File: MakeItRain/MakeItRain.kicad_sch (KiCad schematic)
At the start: 26 parts, among them IC1 OPA2340PA, IC2 LM2597MX-5.0_NOPB, J1 Conn_02x16_Odd_Even, J2 Conn_02x19_Odd_Even, J3 Conn_01x19, P1 Screw_Terminal_01x02, Q1 IRF9Z34NPBF, U1 178.6165.0001

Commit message: wip for hardware
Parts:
- removed C1, C2: 0.1uF, Capacitor_THT:C_Disc_D4.7mm_W2.5mm_P5.00mm, symbol Device:C
- removed C3: 68uF, Capacitor_THT:CP_Radial_D8.0mm_P3.50mm, symbol Device:CP1
- removed C4: 120uF, Capacitor_THT:CP_Radial_D8.0mm_P3.50mm, symbol Device:CP1
- removed D1: 1N5817, Diode_THT:D_DO-41_SOD81_P10.16mm_Horizontal, symbol Diode:1N5817
- removed IC1: OPA2340PA, SamacSys_Parts:DIP794W53P254L959H508Q8N, symbol SamacSys_Parts:OPA2340PA
- removed IC2: LM2597MX-5.0_NOPB, SamacSys_Parts:SOIC127P600X175-8N, symbol SamacSys_Parts:LM2597MX-5.0_NOPB
- removed IC?: LTV-846S, SOP254P1016X460-16N, symbol Samac_Sys:LTV-846S
- removed IC?: SN7404DR, SOIC127P600X175-14N, symbol Samac_Sys:SN7404DR
- removed L1: 150uH, Inductor_THT:L_Axial_L6.6mm_D2.7mm_P10.16mm_Horizontal_Vishay_IM-2, symbol Device:L
- removed P1: Screw_Terminal_01x02, TerminalBlock_Phoenix:TerminalBlock_Phoenix_MKDS-1,5-2-5.08_1x02_P5.08mm_Horizontal, symbol Connector:Screw_Terminal_01x02
- removed Q1: IRF9Z34NPBF, SamacSys_Parts:TO254P469X1042X1967-3P, symbol SamacSys_Parts:IRF9Z34NPBF
- removed R1, R6: 10k, Resistor_THT:R_Axial_DIN0207_L6.3mm_D2.5mm_P5.08mm_Vertical, symbol Device:R
- removed R5: 47k, Resistor_THT:R_Axial_DIN0207_L6.3mm_D2.5mm_P5.08mm_Vertical, symbol Device:R
- removed U1: 178.6165.0001, SamacSys_Parts:17861650001, symbol SamacSys_Parts:178.6165.0001
- added C9: 0.1uF, Capacitor_THT:C_Rect_L9.0mm_W3.6mm_P7.50mm_MKT, symbol Device:C
- added IC1: DS3231SN#, SamacSys_Parts:SOIC127P1032X265-16N, symbol SamacSys_Parts:DS3231SN#
- added U2: S8411-45R, SamacSys_Parts:S8411-45R_1, symbol SamacSys_Parts:S8411-45R
- R3: value 120k -> 10k; footprint Resistor_THT:R_Axial_DIN0207_L6.3mm_D2.5mm_P5.08mm_Vertical -> Resistor_THT:R_Axial_DIN0207_L6.3mm_D2.5mm_P2.54mm_Vertical
- R4: value 15k -> 10k; footprint Resistor_THT:R_Axial_DIN0207_L6.3mm_D2.5mm_P5.08mm_Vertical -> Resistor_THT:R_Axial_DIN0207_L6.3mm_D2.5mm_P2.54mm_Vertical
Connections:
- net +3V3: now also R3.1, R4.1, C9.1, IC1.2 (VCC)
- net +VDC: no longer R3.1
- net D4: no longer J3.13 (Pin_13)
- net GND: now also C9.2, IC1.10 (N.C._6), IC1.11 (N.C._7), IC1.12 (N.C._8), IC1.13 (GND), IC1.5 (N.C._1), IC1.6 (N.C._2), IC1.7 (N.C._3), IC1.8 (N.C._4), IC1.9 (N.C._5), U2.2 (-); no longer R4.2
- net SCL: now reaches R3.2
- net SCL: now also IC1.16 (SCL); no longer R4.1
- new net RTCBattLevel: IC1.14 (VBAT), U2.1 (+)
- new net SDA: IC1.15 (SDA), R4.2
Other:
- added sheet InputIsolation (InputIsolation.kicad_sch)
- added sheet Power (Power.kicad_sch)
- added sheet Voltage Sensors (VoltageSensors.kicad_sch)
- moved on the sheet: J1, J2, J3, R2, Z1, Z2, Z3, Z4

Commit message: wip
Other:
- sheet InputIsolation ports: added 1in, 1out, 2in, 2out, 3in, 3out, 4in, 4out; removed none
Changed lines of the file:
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@@
       (effects (font (size 1.27 1.27)) (justify left top))
+    )
+    (pin "2out" input (at 146.05 59.69 0)
+      (effects (font (size 1.27 1.27)) (justify right))
+    )
+    (pin "1out" input (at 146.05 57.15 0)
+      (effects (font (size 1.27 1.27)) (justify right))
+    )
+    (pin "3out" input (at 146.05 62.23 0)
+      (effects (font (size 1.27 1.27)) (justify right))
+    )
+    (pin "4out" input (at 146.05 64.77 0)
+      (effects (font (size 1.27 1.27)) (justify right))
+    )
+    (pin "4in" input (at 129.54 64.77 180)
+      (effects (font (size 1.27 1.27)) (justify left))
+    )
+    (pin "1in" input (at 129.54 57.15 180)
+      (effects (font (size 1.27 1.27)) (justify left))
+    )
+    (pin "3in" input (at 129.54 62.23 180)
+      (effects (font (size 1.27 1.27)) (justify left))
+    )
+    (pin "2in" input (at 129.54 59.69 180)
+      (effects (font (size 1.27 1.27)) (justify left))
     )
   )

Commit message: wip for input fix.
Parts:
- removed R2: 22k, Resistor_THT:R_Axial_DIN0207_L6.3mm_D2.5mm_P5.08mm_Vertical, symbol Device:R
- renumbered C9 to C1, R3 to R1, R4 to R2, U2 to U1
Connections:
- net SCL is gone; now on net D22: IC1.16 (SCL), R1.2
- net SDA is gone; now on net D21: IC1.15 (SDA), R2.2
- net SVN is gone; now on net D39: J2.7 (Pin_7), J2.8 (Pin_8)
- net +5V: now also J1.13 (Pin_13), J1.15 (Pin_15), J1.17 (Pin_17)
- net D0: now also J1.28 (Pin_28); no longer J1.24 (Pin_24)
- net D15: no longer J1.26 (Pin_26)
- net D16: no longer J1.20 (Pin_20)
- net D17: no longer J1.13 (Pin_13)
- net D18: now also J1.12 (Pin_12); no longer J1.18 (Pin_18)
- net D19: now also J1.10 (Pin_10); no longer J1.14 (Pin_14)
- net D2: no longer J1.32 (Pin_32)
- net D21: now also J1.24 (Pin_24), J1.6 (Pin_6); no longer J1.10 (Pin_10)
- net D22: now also J1.4 (Pin_4); no longer J1.6 (Pin_6)
- net D23: now also J1.8 (Pin_8); no longer J1.30 (Pin_30)
- net D25: now also J1.22 (Pin_22); no longer J1.12 (Pin_12)
- net D26: no longer J1.16 (Pin_16)
- net D32: now also J1.18 (Pin_18); no longer J1.4 (Pin_4)
- net D33: now also J1.20 (Pin_20); no longer J1.8 (Pin_8)
- net D35: now also J1.16 (Pin_16)
- net D4: now also J1.26 (Pin_26), J3.13 (Pin_13); no longer J1.22 (Pin_22)
- net D5: now also J1.14 (Pin_14); no longer J1.28 (Pin_28)
- net RX: now also J1.32 (Pin_32); no longer J1.15 (Pin_15)
- net TX: now also J1.30 (Pin_30); no longer J1.17 (Pin_17)
- net RTCBattLevel renamed D39
- net SVP renamed D36

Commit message: wip for layout
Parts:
- removed J1: Conn_02x16_Odd_Even, Connector_PinSocket_2.54mm:PinSocket_2x16_P2.54mm_Vertical, symbol Connector_Generic:Conn_02x16_Odd_Even
- added D1: LED, LED_THT:LED_D3.0mm, symbol Device:LED
- added J1: Conn_02x15_Odd_Even, Connector_PinHeader_2.54mm:PinHeader_2x15_P2.54mm_Vertical, symbol Connector_Generic:Conn_02x15_Odd_Even
- added R3: 10k, Resistor_THT:R_Axial_DIN0207_L6.3mm_D2.5mm_P2.54mm_Vertical, symbol Device:R
- added R4: 330, Resistor_THT:R_Axial_DIN0207_L6.3mm_D2.5mm_P2.54mm_Vertical, symbol Device:R
- added S1: TS02-66-160-BK-260-LCR-D, TS0266160BK260LCRD, symbol Samac_Sys:TS02-66-160-BK-260-LCR-D
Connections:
- net +3V3: now also J1.2 (Pin_2), J1.4 (Pin_4), S1.2 (NO_2)
- net +5V: now also J1.11 (Pin_11), J1.13 (Pin_13), J1.15 (Pin_15)
- net +VDC: now also J1.1 (Pin_1), J1.3 (Pin_3), J1.5 (Pin_5), J1.7 (Pin_7), J1.9 (Pin_9)
- net D0: now also J1.26 (Pin_26)
- net D13: no longer J2.29 (Pin_29), J2.30 (Pin_30)
- net D18: now also J1.10 (Pin_10)
- net D19: now also J1.8 (Pin_8)
- net D21: now also D1.2 (A), J1.22 (Pin_22)
- net D22: now also R3.1, S1.4 (COM_2)
- net D23: now also J1.6 (Pin_6)
- net D25: now also J1.20 (Pin_20)
- net D32: now also J1.16 (Pin_16)
- net D33: now also J1.18 (Pin_18)
- net D35: now also J1.14 (Pin_14)
- net D4: now also J1.24 (Pin_24)
- net D5: now also J1.12 (Pin_12)
- net GND: now also J1.17 (Pin_17), J1.19 (Pin_19), J1.21 (Pin_21), J1.23 (Pin_23), J1.25 (Pin_25), J1.27 (Pin_27), J1.29 (Pin_29), R3.2, R4.2
- net RX: now also J1.30 (Pin_30)
- net SD2: no longer J2.31 (Pin_31), J2.32 (Pin_32)
- net SD3: no longer J2.33 (Pin_33), J2.34 (Pin_34)
- net TX: now also J1.28 (Pin_28)
- new net: D1.1 (K), R4.1
- no-connect marks 11 -> 19

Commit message: pre routing
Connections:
- net +3V3: no longer J1.4 (Pin_4)
- new net AuxVoltage: J1.4 (Pin_4)
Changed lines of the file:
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@@
   (junction (at 36.83 175.26) (diameter 0) (color 0 0 0 0)
-  )
-  (junction (at 161.29 125.73) (diameter 0) (color 0 0 0 0)
   )
   (junction (at 25.4 167.64) (diameter 0) (color 0 0 0 0)
@@
     (stroke (width 0) (type default) (color 0 0 0 0))
   )
+  (wire (pts (xy 161.29 128.27) (xy 177.8 128.27))
+    (stroke (width 0) (type default) (color 0 0 0 0))
+  )
   (wire (pts (xy 224.79 38.735) (xy 224.79 43.815))
     (stroke (width 0) (type default) (color 0 0 0 0))
@@
   )
   (wire (pts (xy 36.83 175.26) (xy 25.4 175.26))
-    (stroke (width 0) (type default) (color 0 0 0 0))
-  )
-  (wire (pts (xy 161.29 125.73) (xy 161.29 128.27))
     (stroke (width 0) (type default) (color 0 0 0 0))
   )
@@
     (property "Intersheet References" "${INTERSHEET_REFS}" (id 0) (at 183.8132 130.7306 0)
       (effects (font (size 1.27 1.27)) (justify left) hide)
+    )
+  )
+  (global_label "AuxVoltage" (shape input) (at 177.8 128.27 0) (fields_autoplaced)
+    (effects (font (size 1.27 1.27)) (justify left))
+    (property "Intersheet References" "${INTERSHEET_REFS}" (id 0) (at 190.4052 128.1906 0)
+      (effects (font (size 1.27 1.27)) (justify right) hide)
     )
   )
@@
       (reference "#PWR046") (unit 1) (value "+3.3V") (footprint "")
     )
-    (path "/356c600f-2a68-48a9-b543-d1d039e7c815/b25a6e7f-ac8f-4fb5-9236-f417632edc9d"
-      (reference "#PWR047") (unit 1) (value "+3.3V") (footprint "")
-    )
     (path "/8d40f71f-a20a-4db7-8103-dcb791f86750/c6d1a5ed-a9f5-400d-9242-15501f9eaaf7"
       (reference "#PWR047") (unit 1) (value "GND") (footprint "")
@@
     )
     (path "/8d40f71f-a20a-4db7-8103-dcb791f86750/5c2fd002-181f-47cf-b659-f3e455c0bf84"
-      (reference "#PWR?") (unit 1) (value "GND") (footprint "")
+      (reference "#PWR0101") (unit 1) (value "GND") (footprint "")
+    )
+    (path "/356c600f-2a68-48a9-b543-d1d039e7c815/b25a6e7f-ac8f-4fb5-9236-f417632edc9d"
+      (reference "#PWR0102") (unit 1) (value "+3.3V") (footprint "")
     )
     (path "/90c4be7f-3410-4327-b602-922129c35c5d"
@@
       (reference "D6") (unit 1) (value "1N4007") (footprint "Diode_THT:D_DO-41_SOD81_P10.16mm_Horizontal")
     )
-    (path "/00000000-0000-0000-0000-00006158b83d/00000000-0000-0000-0000-0000615dbdb1"
+    (path "/00000000-0000-0000-0000-00006158b957/00000000-0000-0000-0000-0000615dbdb1"
       (reference "D7") (unit 1) (value "STPS3150RL") (footprint "Diode_THT:D_DO-201_P15.24mm_Horizontal")
     )
@@
       (reference "D8") (unit 1) (value "1N4007") (footprint "Diode_THT:D_DO-41_SOD81_P10.16mm_Horizontal")
     )
-    (path "/00000000-0000-0000-0000-00006158b957/00000000-0000-0000-0000-0000615dbdb1"
+    (path "/00000000-0000-0000-0000-00006158b83d/00000000-0000-0000-0000-0000615dbdb1"
       (reference "D9") (unit 1) (value "STPS3150RL") (footprint "Diode_THT:D_DO-201_P15.24mm_Horizontal")
     )
@@
       (reference "J3") (unit 1) (value "Conn_01x19") (footprint "Connector_PinSocket_2.54mm:PinSocket_1x19_P2.54mm_Vertical")
     )
-    (path "/8d40f71f-a20a-4db7-8103-dcb791f86750/6020cd58-4f88-49ce-8ea8-42dd43bbb15b"
-      (reference "J4") (unit 1) (value "Conn_01x03") (footprint "Connector_PinHeader_2.54mm:PinHeader_1x03_P2.54mm_Vertical")
+    (path "/8d40f71f-a20a-4db7-8103-dcb791f86750/fa1e7186-4f1e-43c0-bd2b-271157226479"
+      (reference "J4") (unit 1) (value "Conn_01x01") (footprint "Connector_PinHeader_2.54mm:PinHeader_1x01_P2.54mm_Vertical")
     )
     (path "/99204adf-a081-4da3-8031-dd03bceb7b2a/543ff046-0771-46a7-8845-3f5ebc2980df"
@@
     )
     (path "/8d40f71f-a20a-4db7-8103-dcb791f86750/c2a57e48-486b-4b03-9956-74f9371d1585"
-      (reference "R?") (unit 1) (value "47k") (footprint "Resistor_THT:R_Axial_DIN0207_L6.3mm_D2.5mm_P2.54mm_Vertical")
+      (reference "R34") (unit 1) (value "47k") (footprint "Resistor_THT:R_Axial_DIN0207_L6.3mm_D2.5mm_P2.54mm_Vertical")
     )
     (path "/8d40f71f-a20a-4db7-8103-dcb791f86750/73b41eb2-3ccf-4143-92fe-caaab34649bf"

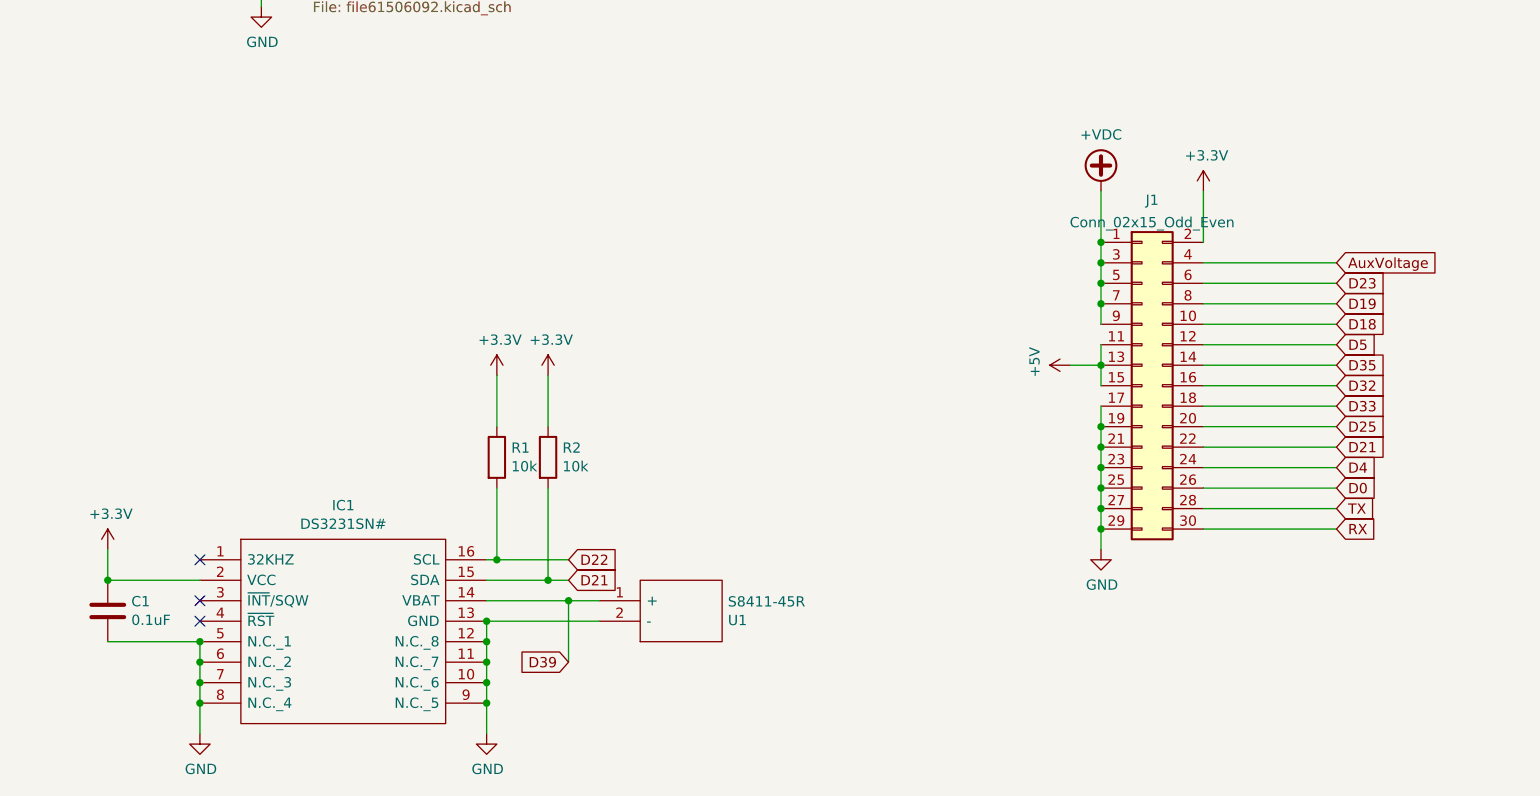
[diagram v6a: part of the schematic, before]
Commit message: wip for removing the external RTC and moving the power stuff around to make it easier to install into enclosure.
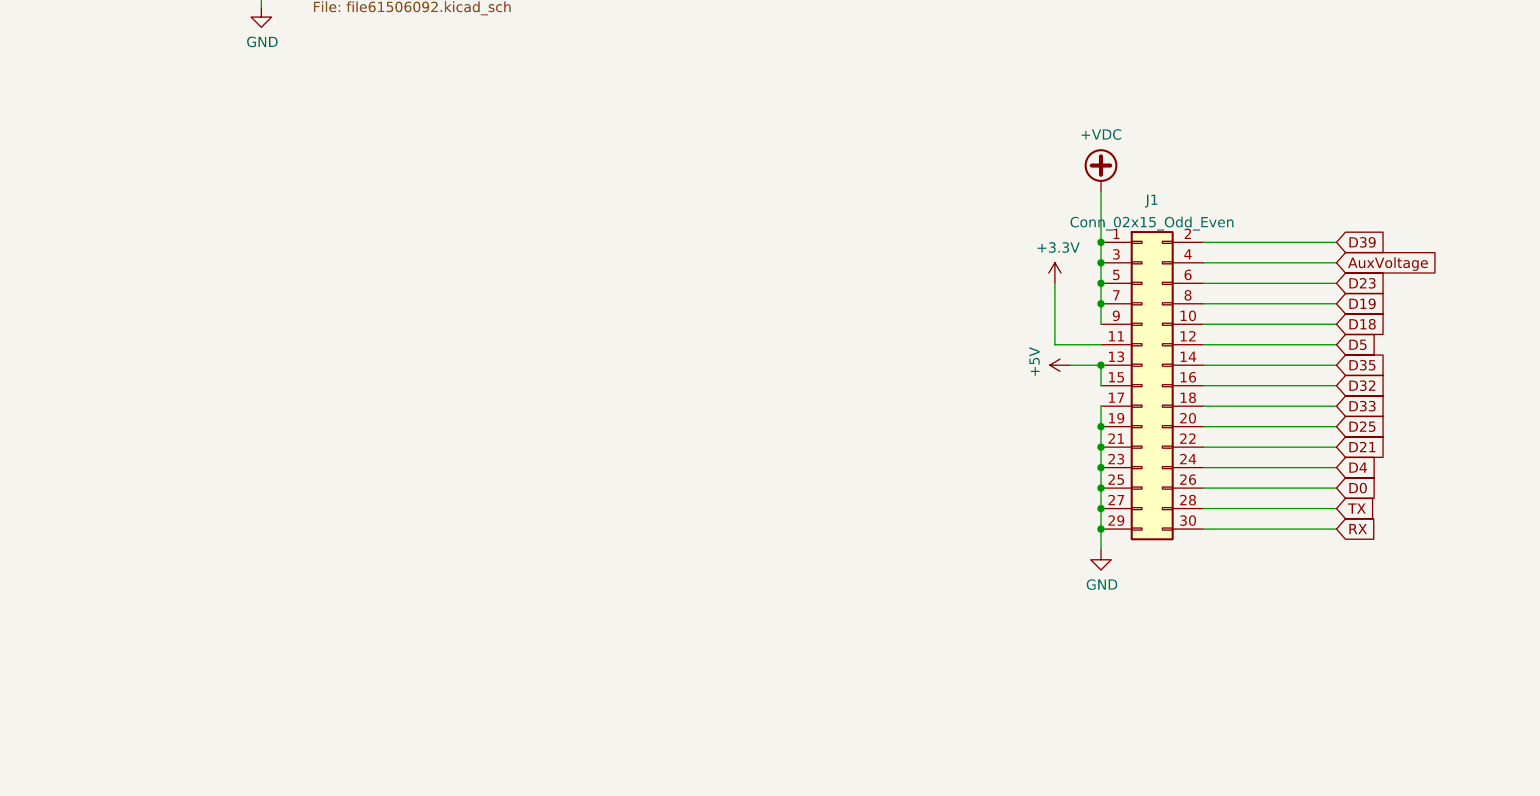
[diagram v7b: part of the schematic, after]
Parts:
- removed C1: 0.1uF, Capacitor_THT:C_Rect_L9.0mm_W3.6mm_P7.50mm_MKT, symbol Device:C
- removed IC1: DS3231SN#, SamacSys_Parts:SOIC127P1032X265-16N, symbol SamacSys_Parts:DS3231SN#
- removed R1, R2: 10k, Resistor_THT:R_Axial_DIN0207_L6.3mm_D2.5mm_P2.54mm_Vertical, symbol Device:R
- removed U1: S8411-45R, SamacSys_Parts:S8411-45R_1, symbol SamacSys_Parts:S8411-45R
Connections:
- net +3V3: now also J1.11 (Pin_11); no longer J1.2 (Pin_2)
- net +5V: no longer J1.11 (Pin_11)
- net D39: now also J1.2 (Pin_2)
- no-connect marks 19 -> 16
